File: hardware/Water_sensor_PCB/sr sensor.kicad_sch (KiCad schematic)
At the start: 12 parts, among them J1 Conn_01x07_Pin, Q1 BPW40, Q2 BPW40, SW1 SW_Nidec_CAS-120A1

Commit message: changed JST connector size, changed silkscreen
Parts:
- J1: footprint Connector_JST:JST_EH_B7B-EH-A_1x07_P2.50mm_Vertical -> Connector_JST:JST_GH_BM07B-GHS-TBT_1x07-1MP_P1.25mm_Vertical
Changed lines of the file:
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@@
 			)
 		)
-		(property "Footprint" "Connector_JST:JST_EH_B7B-EH-A_1x07_P2.50mm_Vertical"
+		(property "Footprint" "Connector_JST:JST_GH_BM07B-GHS-TBT_1x07-1MP_P1.25mm_Vertical"
 			(at 170.18 96.52 0)
 			(effects

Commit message: feat: Cleanup files and start redesign
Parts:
- removed Q1, Q2: BPW40, LED_THT:LED_D5.0mm_Clear, symbol Sensor_Optical:BPW40
- J1: footprint Connector_JST:JST_GH_BM07B-GHS-TBT_1x07-1MP_P1.25mm_Vertical -> Connector_JST:JST_XH_B7B-XH-A_1x07_P2.50mm_Vertical; symbol Connector:Conn_01x07_Pin -> Connector_Generic:Conn_01x07
- SW1: footprint Connector_PinHeader_2.54mm:PinHeader_1x03_P2.54mm_Vertical -> Connector_JST:JST_XH_B3B-XH-A_1x03_P2.50mm_Vertical
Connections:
- net +5V: now also J1.7 (Pin_7); no longer J1.1 (Pin_1)
- net CH1: now also J1.3 (Pin_3); no longer J1.5 (Pin_5)
- net DRAIN1: now also J1.6 (Pin_6); no longer J1.2 (Pin_2)
- net DRAIN2: now also J1.5 (Pin_5); no longer J1.3 (Pin_3)
- net GND: now also J1.1 (Pin_1); no longer J1.7 (Pin_7)
- net SWITCH: now also J1.2 (Pin_2); no longer J1.6 (Pin_6)

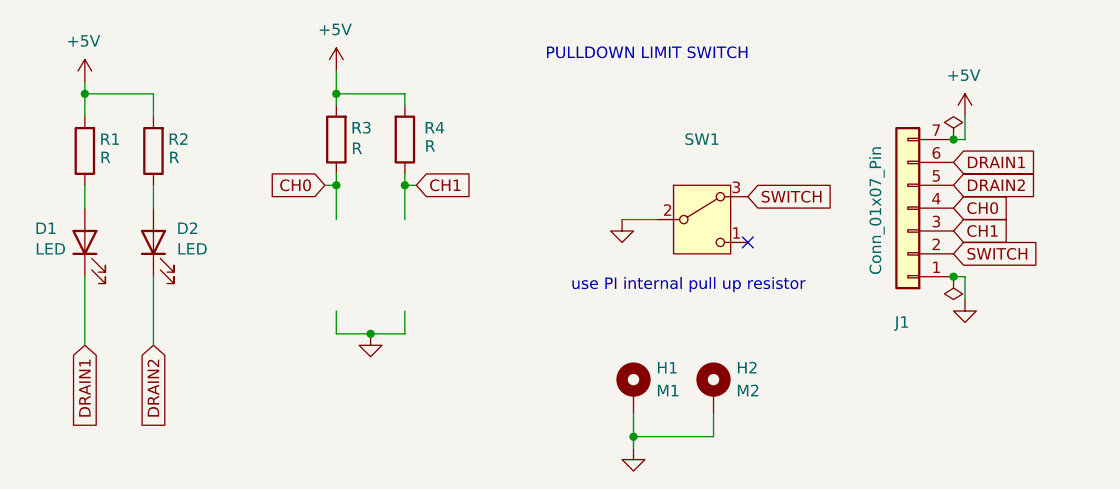
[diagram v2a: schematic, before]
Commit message: feat: Cleanup and redesign of sensor pcb
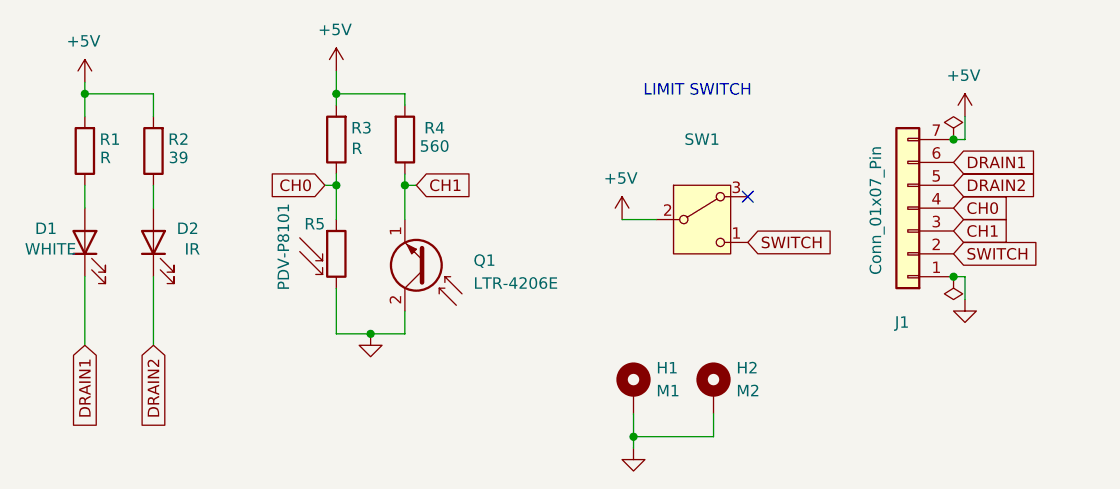
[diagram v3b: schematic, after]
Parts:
- added Q1: LTR-4206E, LED_THT:LED_D3.0mm, symbol Device:Q_Photo_NPN_EC
- added R5: PDV-P8101, OptoDevice:R_LDR_5.1x4.3mm_P3.4mm_Vertical, symbol Device:R_Photo
- D1: value LED -> WHITE
- D2: value LED -> IR
- H1, H2: footprint MountingHole:MountingHole_2.2mm_M2_Pad_Via -> MountingHole:MountingHole_3.2mm_M3_Pad_Via
- J1: footprint Connector_JST:JST_XH_B7B-XH-A_1x07_P2.50mm_Vertical -> Connector_JST:JST_ZH_B7B-ZR_1x07_P1.50mm_Vertical
- R1, R3: footprint Resistor_SMD:R_0805_2012Metric -> Resistor_SMD:R_0805_2012Metric_Pad1.20x1.40mm_HandSolder
- R2: value R -> 39; footprint Resistor_SMD:R_0805_2012Metric -> Resistor_SMD:R_0805_2012Metric_Pad1.20x1.40mm_HandSolder
- R4: value R -> 560; footprint Resistor_SMD:R_0805_2012Metric -> Resistor_SMD:R_0805_2012Metric_Pad1.20x1.40mm_HandSolder
- SW1: footprint Connector_JST:JST_XH_B3B-XH-A_1x03_P2.50mm_Vertical -> Connector_JST:JST_ZH_B3B-ZR_1x03_P1.50mm_Vertical
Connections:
- net +5V: now also SW1.2 (B)
- net CH0: now also R5.1
- net CH1: now also Q1.1 (E)
- net GND: now also Q1.2 (C), R5.2; no longer SW1.2 (B)
- net SWITCH: now also SW1.1 (C); no longer SW1.3 (A)
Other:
- note added: "LIMIT SWITCH"
- note removed: "PULLDOWN LIMIT SWITCH"
- note removed: "use PI internal pull up resistor"
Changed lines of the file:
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@@
 	(generator_version "9.99")
 	(paper "A4")
-	(text "PULLDOWN LIMIT SWITCH\n"
-		(exclude_from_sim no)
-		(at 136.144 75.692 0)
-		(effects
-			(font
-				(size 1.27 1.27)
-			)
-		)
-	)
-	(text "use PI internal pull up resistor\n"
-		(exclude_from_sim no)
-		(at 140.716 101.346 0)
+	(text "LIMIT SWITCH\n"
+		(exclude_from_sim no)
+		(at 141.732 79.756 0)
 		(effects
 			(font
@@
 	)
 	(no_connect
-		(at 147.32 96.52)
+		(at 147.32 91.44)
 	)
 	(wire
@@
 	(wire
 		(pts
-			(xy 101.6 104.14) (xy 101.6 106.68)
+			(xy 101.6 101.6) (xy 101.6 106.68)
 		)
 		(stroke
@@
 		)
 	)
-	(global_label "SWITCH"
-		(shape input)
-		(at 147.32 91.44 0)
-		(fields_autoplaced yes)
-		(effects
-			(font
-				(size 1.27 1.27)
-			)
-			(justify left)
-		)
-		(property "Intersheetrefs" "${INTERSHEET_REFS}"
-			(at 157.139 91.44 0)
-			(hide yes)
-			(effects
-				(font
-					(size 1.27 1.27)
-				)
-				(justify left)
-			)
-		)
-	)
 	(global_label "CH1"
 		(shape input)
@@
 		)
 	)
+	(global_label "SWITCH"
+		(shape input)
+		(at 147.32 96.52 0)
+		(fields_autoplaced yes)
+		(effects
+			(font
+				(size 1.27 1.27)
+			)
+			(justify left)
+		)
+		(property "Intersheetrefs" "${INTERSHEET_REFS}"
+			(at 157.139 96.52 0)
+			(hide yes)
+			(effects
+				(font
+					(size 1.27 1.27)
+				)
+				(justify left)
+			)
+		)
+	)
 	(global_label "DRAIN1"
 		(shape input)
@@
 			)
 		)
-		(property "Footprint" "Resistor_SMD:R_0805_2012Metric"
+		(property "Footprint" "Resistor_SMD:R_0805_2012Metric_Pad1.20x1.40mm_HandSolder"
 			(at 75.438 86.36 90)
 			(hide yes)
@@
 	)
 	(symbol
+		(lib_id "power:+3.3V")
+		(at 133.35 93.98 0)
+		(unit 1)
+		(exclude_from_sim no)
+		(in_bom yes)
+		(on_board yes)
+		(dnp no)
+		(property "Reference" "#PWR07"
+			(at 133.35 97.79 0)
+			(hide yes)
+			(effects
+				(font
+					(size 1.27 1.27)
+				)
+			)
+		)
+		(property "Value" "+5V"
+			(at 131.318 89.408 0)
+			(effects
+				(font
+					(size 1.27 1.27)
+				)
+				(justify left)
+			)
+		)
+		(property "Footprint" ""
+			(at 133.35 93.98 0)
+			(hide yes)
+			(effects
+				(font
+					(size 1.27 1.27)
+				)
+			)
+		)
+		(property "Datasheet" ""
+			(at 133.35 93.98 0)
+			(hide yes)
+			(effects
+				(font
+					(size 1.27 1.27)
+				)
+			)
+		)
+		(property "Description" "Power symbol creates a global label with name \"+3.3V\""
+			(at 133.35 93.98 0)
+			(hide yes)
+			(effects
+				(font
+					(size 1.27 1.27)
+				)
+			)
+		)
+		(pin "1"
+		)
+		(instances
+			(project "sr sensor"
+				(path "/94f8d93d-a372-45d1-bb9b-ef3aed27d49c"
+					(reference "#PWR07")
+					(unit 1)
+				)
+			)
+		)
+	)
+	(symbol
 		(lib_id "Device:R")
 		(at 109.22 85.09 0)
@@
 			)
 		)
-		(property "Value" "R"
-			(at 112.014 85.852 0)
-			(effects
-				(font
-					(size 1.27 1.27)
-				)
-			)
-		)
-		(property "Footprint" "Resistor_SMD:R_0805_2012Metric"
+		(property "Value" "560"
+			(at 112.522 85.852 0)
+			(effects
+				(font
+					(size 1.27 1.27)
+				)
+			)
+		)
+		(property "Footprint" "Resistor_SMD:R_0805_2012Metric_Pad1.20x1.40mm_HandSolder"
 			(at 107.442 85.09 90)
 			(hide yes)
@@
 	)
 	(symbol
-		(lib_id "power:GND")
-		(at 133.35 93.98 0)
+		(lib_id "Device:R_Photo")
+		(at 101.6 97.79 0)
 		(unit 1)
 		(exclude_from_sim no)
@@
 		(on_board yes)
 		(dnp no)
-		(fields_autoplaced yes)
-		(property "Reference" "#PWR07"
-			(at 133.35 100.33 0)
-			(hide yes)
-			(effects
-				(font
-					(size 1.27 1.27)
-				)
-			)
-		)
-		(property "Value" "GND"
-			(at 133.35 99.06 0)
-			(hide yes)
-			(effects
-				(font
-					(size 1.27 1.27)
-				)
-			)
-		)
-		(property "Footprint" ""
-			(at 133.35 93.98 0)
-			(hide yes)
-			(effects
-				(font
-					(size 1.27 1.27)
-				)
-			)
-		)
-		(property "Datasheet" ""
-			(at 133.35 93.98 0)
-			(hide yes)
-			(effects
-				(font
-					(size 1.27 1.27)
-				)
-			)
-		)
-		(property "Description" "Power symbol creates a global label with name \"GND\" , ground"
-			(at 133.35 93.98 0)
-			(hide yes)
-			(effects
-				(font
-					(size 1.27 1.27)
-				)
-			)
-		)
-		(pin "1"
-		)
-		(instances
-			(project "sr sensor"
-				(path "/94f8d93d-a372-45d1-bb9b-ef3aed27d49c"
-					(reference "#PWR07")
+		(property "Reference" "R5"
+			(at 98.044 94.488 0)
+			(effects
+				(font
+					(size 1.27 1.27)
+				)
+				(justify left)
+			)
+		)
+		(property "Value" "PDV-P8101"
+			(at 95.758 101.854 90)
+			(effects
+				(font
+					(size 1.27 1.27)
+				)
+				(justify left)
+			)
+		)
+		(property "Footprint" "OptoDevice:R_LDR_5.1x4.3mm_P3.4mm_Vertical"
+			(at 102.87 104.14 90)
+			(hide yes)
+			(effects
+				(font
+					(size 1.27 1.27)
+				)
+				(justify left)
+			)
+		)
+		(property "Datasheet" "~"
+			(at 101.6 99.06 0)
+			(hide yes)
+			(effects
+				(font
+					(size 1.27 1.27)
+				)
+			)
+		)
+		(property "Description" "Photoresistor"
+			(at 101.6 97.79 0)
+			(hide yes)
+			(effects
+				(font
+					(size 1.27 1.27)
+				)
+			)
+		)
+		(pin "1"
+		)
+		(pin "2"
+		)
+		(instances
+			(project ""
+				(path "/94f8d93d-a372-45d1-bb9b-ef3aed27d49c"
+					(reference "R5")
 					(unit 1)
 				)
@@
 			)
 		)
-		(property "Footprint" "Connector_JST:JST_XH_B7B-XH-A_1x07_P2.50mm_Vertical"
+		(property "Footprint" "Connector_JST:JST_ZH_B7B-ZR_1x07_P1.50mm_Vertical"
 			(at 165.1 92.71 0)
 			(hide yes)
@@
 			)
 		)
-		(property "Value" "LED"
+		(property "Value" "IR"
 			(at 85.598 97.282 90)
 			(effects
@@
 			)
 		)
-		(property "Footprint" "MountingHole:MountingHole_2.2mm_M2_Pad_Via"
+		(property "Footprint" "MountingHole:MountingHole_3.2mm_M3_Pad_Via"
 			(at 134.62 113.03 0)
 			(hide yes)
@@
 			)
 		)
-		(property "Value" "LED"
+		(property "Value" "WHITE"
 			(at 69.85 97.282 90)
 			(effects
@@
 			)
 		)
-		(property "Footprint" "Connector_JST:JST_XH_B3B-XH-A_1x03_P2.50mm_Vertical"
+		(property "Footprint" "Connector_JST:JST_ZH_B3B-ZR_1x03_P1.50mm_Vertical"
 			(at 142.24 104.14 0)
 			(hide yes)
@@
 	)
 	(symbol
+		(lib_id "Device:Q_Photo_NPN_EC")
+		(at 111.76 99.06 180)
+		(unit 1)
+		(exclude_from_sim no)
+		(in_bom yes)
+		(on_board yes)
+		(dnp no)
+		(fields_autoplaced yes)
+		(property "Reference" "Q1"
+			(at 116.84 98.5392 0)
+			(effects
+				(font
+					(size 1.27 1.27)
+				)
+				(justify right)
+			)
+		)
+		(property "Value" "LTR-4206E"
+			(at 116.84 101.0792 0)
+			(effects
+				(font
+					(size 1.27 1.27)
+				)
+				(justify right)
+			)
+		)
+		(property "Footprint" "LED_THT:LED_D3.0mm"
+			(at 106.68 101.6 0)
+			(hide yes)
+			(effects
+				(font
+					(size 1.27 1.27)
+				)
+			)
+		)
+		(property "Datasheet" "~"
+			(at 111.76 99.06 0)
+			(hide yes)
+			(effects
+				(font
+					(size 1.27 1.27)
+				)
+			)
+		)
+		(property "Description" "NPN phototransistor, emitter/collector"
+			(at 111.76 99.06 0)
+			(hide yes)
+			(effects
+				(font
+					(size 1.27 1.27)
+				)
+			)
+		)
+		(pin "1"
+		)
+		(pin "2"
+		)
+		(instances
+			(project ""
+				(path "/94f8d93d-a372-45d1-bb9b-ef3aed27d49c"
+					(reference "Q1")
+					(unit 1)
+				)
+			)
+		)
+	)
+	(symbol
 		(lib_id "Device:R")
 		(at 101.6 85.09 180)
@@
 			)
 		)
-		(property "Footprint" "Resistor_SMD:R_0805_2012Metric"
+		(property "Footprint" "Resistor_SMD:R_0805_2012Metric_Pad1.20x1.40mm_HandSolder"
 			(at 103.378 85.09 90)
 			(hide yes)
@@
 			)
 		)
-		(property "Footprint" "MountingHole:MountingHole_2.2mm_M2_Pad_Via"
+		(property "Footprint" "MountingHole:MountingHole_3.2mm_M3_Pad_Via"
 			(at 143.51 113.03 0)
 			(hide yes)
@@
 			)
 		)
-		(property "Value" "R"
-			(at 83.566 87.122 0)
-			(effects
-				(font
-					(size 1.27 1.27)
-				)
-			)
-		)
-		(property "Footprint" "Resistor_SMD:R_0805_2012Metric"
+		(property "Value" "39"
+			(at 84.074 87.122 0)
+			(effects
+				(font
+					(size 1.27 1.27)
+				)
+			)
+		)
+		(property "Footprint" "Resistor_SMD:R_0805_2012Metric_Pad1.20x1.40mm_HandSolder"
 			(at 83.058 86.36 90)
 			(hide yes)
